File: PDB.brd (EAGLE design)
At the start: 125.9 x 103 mm, 84 parts

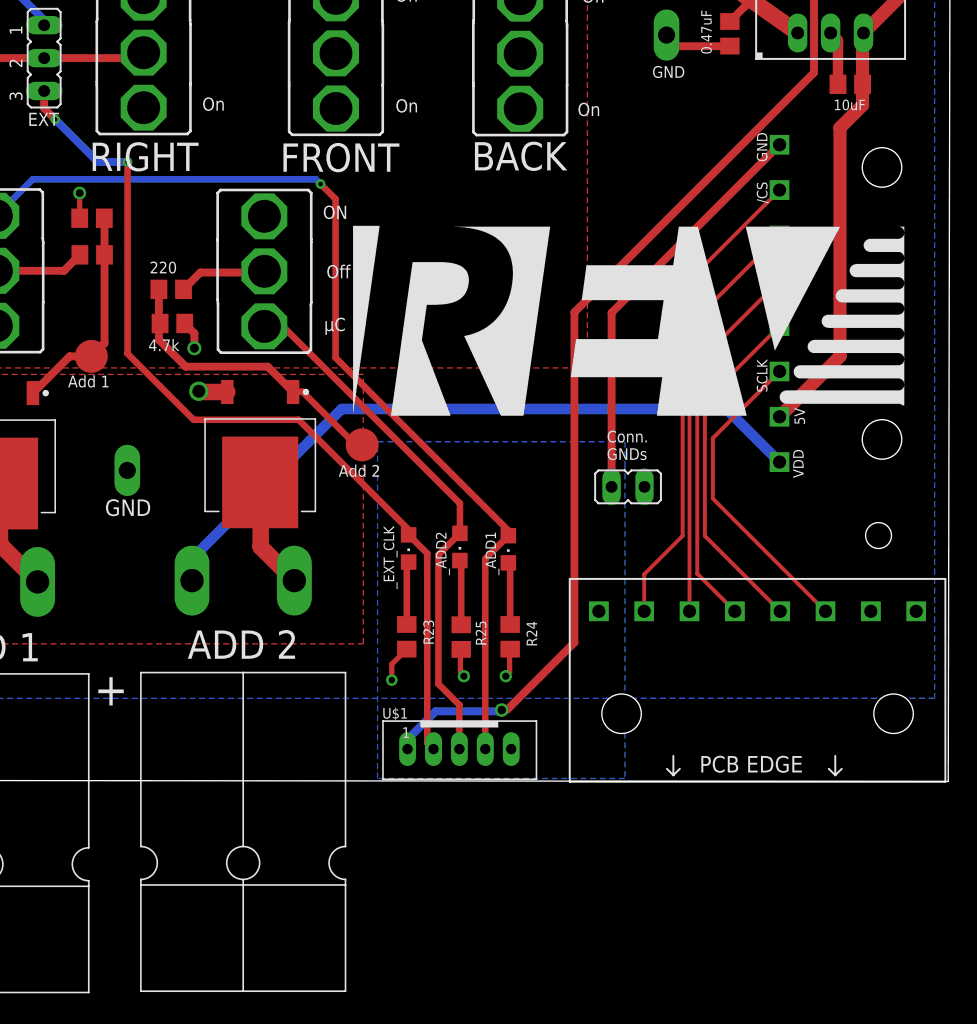
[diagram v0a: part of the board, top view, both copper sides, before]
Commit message: Deleted SPI, ADD2
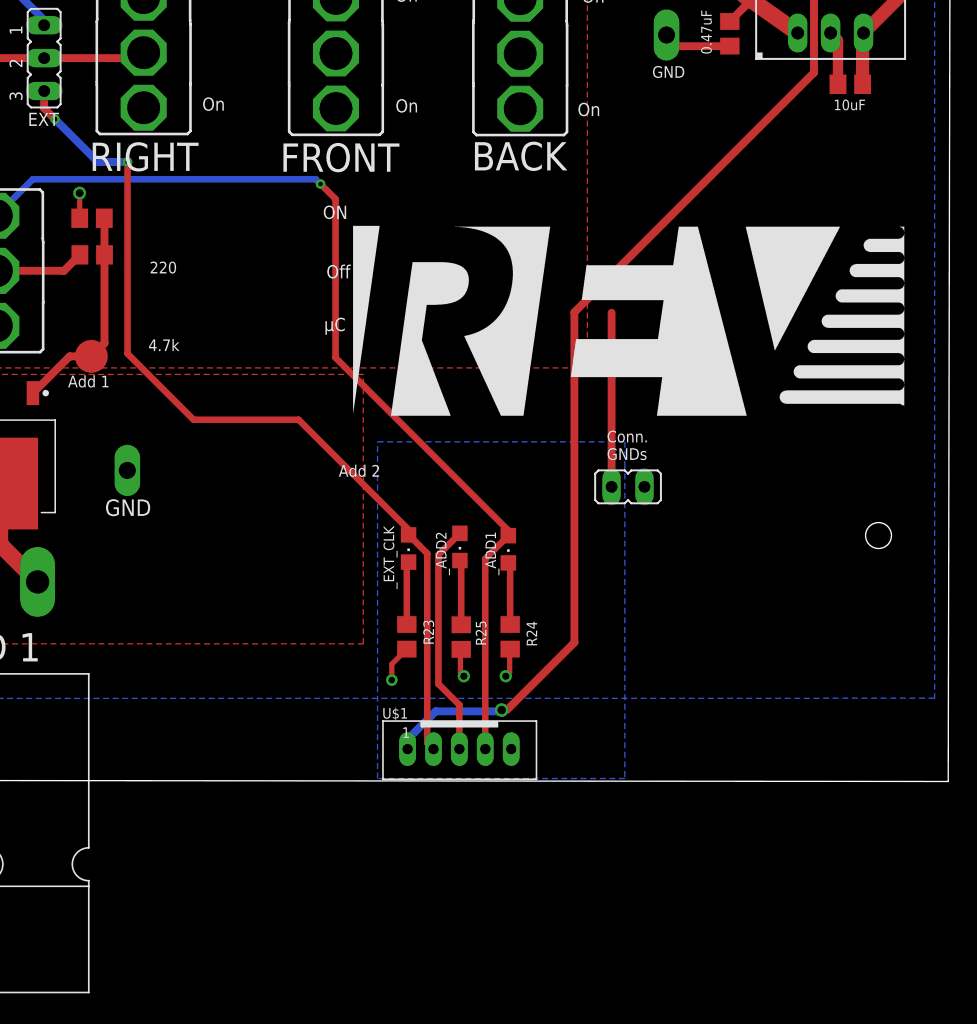
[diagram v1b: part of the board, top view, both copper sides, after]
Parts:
- removed ADD2: NCV8405ADPAK-3PIN, master_library:TO254P1054X240-3
- removed ADD2_: (no value), switch:M9040P
- removed ADD2_OUT: POWERPOLE_POWER25A_HORIZONTAL_G2, powerpoles:POWERPOLE_PAIR_25A_HORIZ_G2
- removed R1: 4.7K, rcl:R0805
- removed R12: 220, rcl:R0805
- removed SPI_IN, SPI_OUT: 8-PIN-MOLEX-RA-FEMALE, master_library:8-PIN-MOLEX
- removed TP2: PTR1B2,54, testpad:B2,54
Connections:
- removed net /CS: SPI_IN.P2, SPI_OUT.P2
- removed net DC: SPI_IN.P4, SPI_OUT.P4
- removed net D_RST: SPI_IN.P3, SPI_OUT.P3
- removed net H6: ADD2_.2, R12.1
- removed net MOSI: SPI_IN.P5, SPI_OUT.P5
- removed net N$7: ADD2.1, R1.1, R12.2, TP2.TP
- removed net N$8: ADD2.3, ADD2_OUT.BLACK
- removed net SCLK: SPI_IN.P6, SPI_OUT.P6
- removed net µC_5V: SPI_IN.P7
- net 10V_REG: no longer ADD2_.3
- net 5V_REG: no longer SPI_OUT.P7
- net GND: no longer ADD2.2, R1.2
- net VDD: no longer ADD2_OUT.RED, SPI_OUT.P8
- net µC_ADD_2: no longer ADD2_.1
- net µC_GND: no longer SPI_IN.P1, SPI_OUT.P1
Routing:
- net VDD: track 76.0 -> 22.5 mm
- net /CS: track 36.8 -> 0.00 mm
- net D_RST: track 31.9 -> 0.00 mm
- net DC: track 29.4 -> 0.00 mm
- net 5V_REG: track 62.0 -> 33.7 mm
- net MOSI: track 26.8 -> 0.00 mm
- net SCLK: track 24.3 -> 0.00 mm
- net µC_ADD_2: track 41.1 -> 18.0 mm
- net N$7: track 23.1 -> 0.00 mm
- net µC_GND: track 39.1 -> 20.8 mm
- net N$8: track 8.67 -> 0.00 mm
- net H6: track 6.82 -> 0.00 mm
- net GND: track 94.1 -> 89.7 mm, vias 22 -> 20
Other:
- board text removed: "/CS"
- board text removed: "5V"
- board text removed: "5V IN"
- board text removed: "ADD 2"
- board text removed: "DC"
- board text removed: "MOSI"
- board text removed: "N/C"
- board text removed: "RST"
- board text removed: "SCLK"
- board text removed: "SPI OUT"
- board text removed: "VDD"

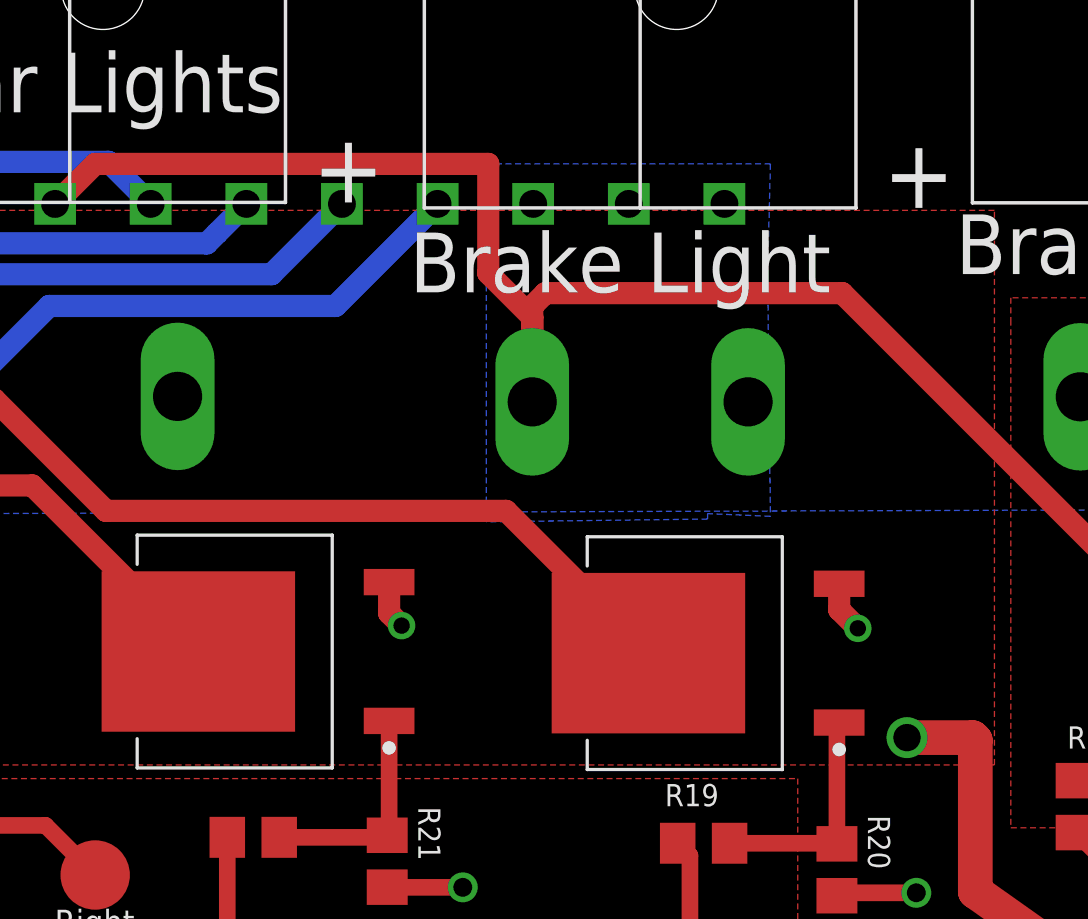
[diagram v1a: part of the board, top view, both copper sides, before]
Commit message: Changed GND to VDD for connector
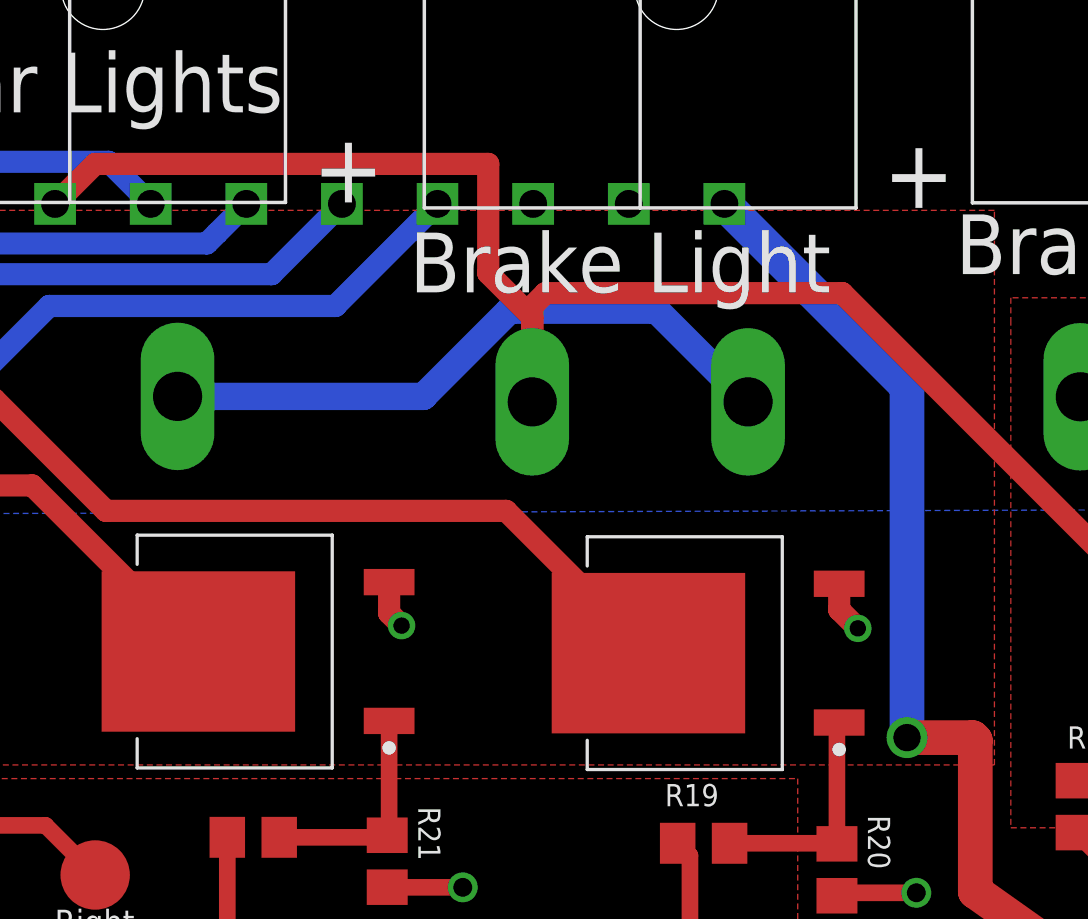
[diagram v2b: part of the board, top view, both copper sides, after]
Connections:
- new net V+: BRAKE_OUT.RED, REARLIGHTS_OUT.RED
- net GND: no longer LIGHTS.P6, LIGHTS.P7, LIGHTS.P8
- net VDD: now also LIGHTS.P6, LIGHTS.P7, LIGHTS.P8; no longer BRAKE_OUT.RED, REARLIGHTS_OUT.RED
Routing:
- net V+: track 0.00 -> 23.6 mm
- net VDD: track 22.5 -> 44.8 mm
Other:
- board text removed: "SPI IN"
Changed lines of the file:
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@@
 <text x="68.1" y="77" size="0.9" layer="25">4.7k</text>
 <text x="48.1" y="77" size="0.9" layer="25">4.7k</text>
-<text x="118.4" y="47" size="1.778" layer="26" rot="MR0">SPI IN</text>
 <text x="104.7" y="55" size="0.8128" layer="26" rot="MR0">µC GND</text>
 <text x="121" y="95.6" size="0.8128" layer="25">10uF</text>
@@
 <contactref element="HAZL_OUT" pad="RED"/>
 <contactref element="HAZR_OUT" pad="RED"/>
-<contactref element="BRAKE_OUT" pad="RED"/>
 <contactref element="HEADLIGHTS_OUT" pad="RED"/>
 <contactref element="C10" pad="+"/>
@@
 <contactref element="WIPER_OUT" pad="RED"/>
 <contactref element="D2" pad="C"/>
-<contactref element="REARLIGHTS_OUT" pad="RED"/>
 <polygon width="0.3048" layer="1" isolate="0.254" rank="2">
 <vertex x="5.7" y="75.2"/>
@@
 <wire x1="114.279484375" y1="103.729484375" x2="114.279484375" y2="104.371015625" width="0.6096" layer="1"/>
 <contactref element="POWER" pad="A"/>
+<contactref element="LIGHTS" pad="P6"/>
+<contactref element="LIGHTS" pad="P7"/>
+<contactref element="LIGHTS" pad="P8"/>
+<wire x1="106" y1="114.1" x2="106" y2="126.952" width="1.27" layer="16"/>
+<wire x1="106" y1="126.952" x2="99.316" y2="133.636" width="1.27" layer="16"/>
 </signal>
 <signal name="N$17">
@@
 <contactref element="TP11" pad="TP"/>
 <contactref element="TP12" pad="TP"/>
-<contactref element="LIGHTS" pad="P8"/>
 <via x="89.74" y="108.62" extent="1-16" drill="0.69"/>
 <via x="106.34" y="108.42" extent="1-16" drill="0.69"/>
@@
 <wire x1="45.4" y1="94" x2="44.6352" y2="94.7648" width="0.8128" layer="1"/>
 <via x="45.4" y="94" extent="1-16" drill="0.6"/>
-<polygon width="0.2032" layer="16" isolate="0.254">
-<vertex x="90.6" y="122"/>
-<vertex x="90.6" y="131"/>
-<vertex x="90.6" y="131.1"/>
-<vertex x="90.6" y="135.1"/>
-<vertex x="101" y="135.1"/>
-<vertex x="100.9" y="131.1"/>
-<vertex x="100.9" y="131"/>
-<vertex x="101" y="122.2"/>
-<vertex x="98.7" y="122.3"/>
-<vertex x="98.7" y="122.1"/>
-</polygon>
-<contactref element="LIGHTS" pad="P7"/>
-<contactref element="LIGHTS" pad="P6"/>
 <wire x1="62.806" y1="87.26" x2="62.806" y2="89.194" width="0.4064" layer="1"/>
 <wire x1="19.244" y1="106.456" x2="20.768" y2="106.456" width="0.6096" layer="1"/>
@@
 <wire x1="113" y1="100.55" x2="112.9896" y2="100.5396" width="1.016" layer="1"/>
 </signal>
+<signal name="V+">
+<contactref element="BRAKE_OUT" pad="RED"/>
+<contactref element="REARLIGHTS_OUT" pad="RED"/>
+<wire x1="79.3" y1="126.59" x2="88.300175" y2="126.59" width="1" layer="16"/>
+<wire x1="88.300175" y1="126.59" x2="91.452575" y2="129.7424" width="1" layer="16"/>
+<wire x1="91.452575" y1="129.7424" x2="96.8296" y2="129.7424" width="1" layer="16"/>
+<wire x1="96.8296" y1="129.7424" x2="100.182" y2="126.39" width="1" layer="16"/>
+</signal>
 </signals>

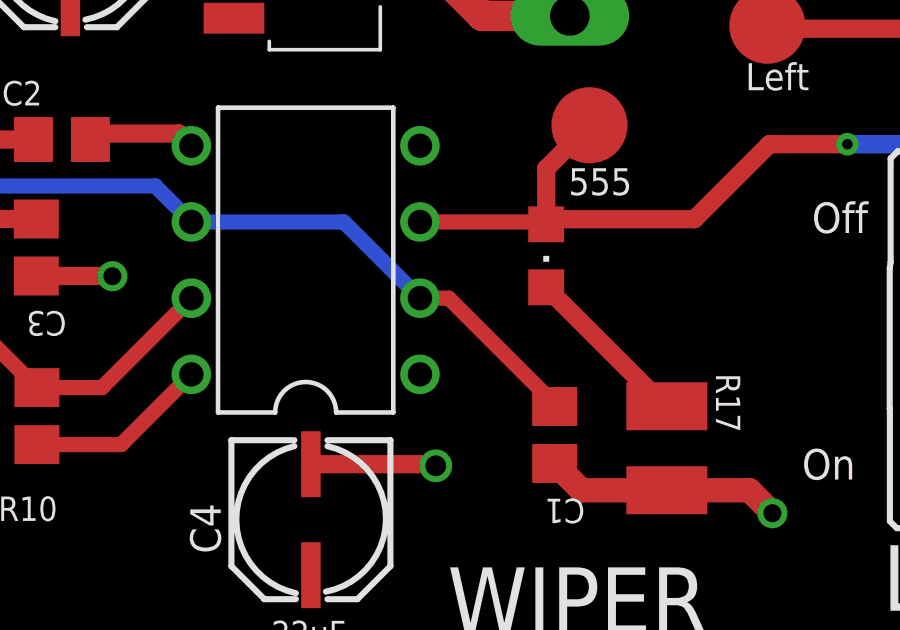
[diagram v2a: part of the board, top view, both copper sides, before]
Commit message: Disconnected 555-timer from the jumper
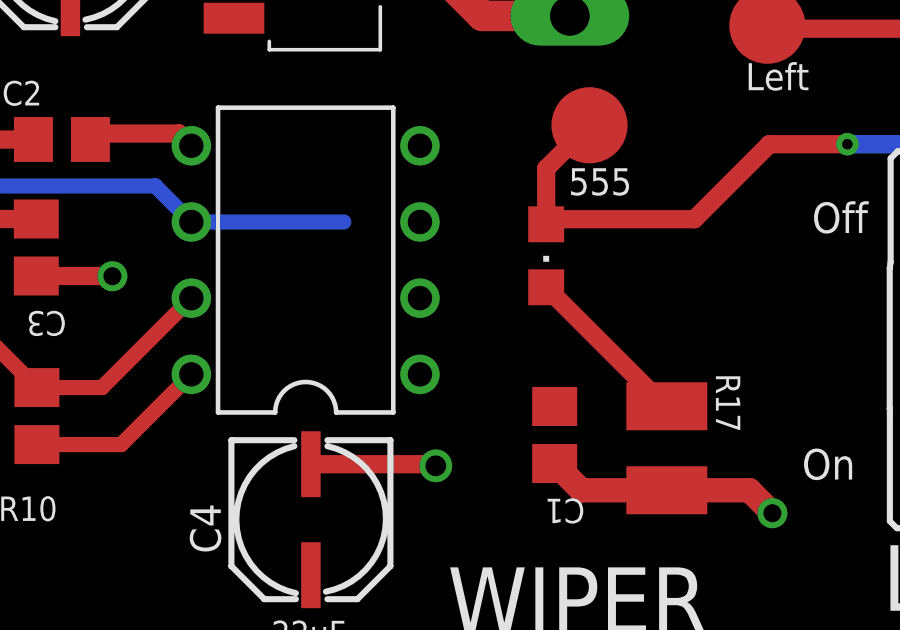
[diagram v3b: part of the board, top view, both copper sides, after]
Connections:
- net 555_OUT: no longer 555.3
- net TR/THR: no longer 555.2, C1.1
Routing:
- net TR/THR: track 39.3 -> 29.6 mm
- net 555_OUT: track 33.5 -> 29.3 mm
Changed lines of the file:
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@@
 <contactref element="JP2" pad="1"/>
 <contactref element="555_CLK_LED" pad="A"/>
-<contactref element="555" pad="3"/>
-<wire x1="33.652" y1="103.708" x2="37.782" y2="103.708" width="0.508" layer="1"/>
 <wire x1="37.86" y1="103.63" x2="37.782" y2="103.708" width="0.6096" layer="1"/>
 <wire x1="38.03" y1="103.8" x2="37.86" y2="103.63" width="0.508" layer="1"/>
@@
 </signal>
 <signal name="TR/THR">
-<contactref element="C1" pad="1"/>
 <contactref element="C3" pad="1"/>
 <contactref element="R11" pad="S"/>
-<contactref element="555" pad="2"/>
 <contactref element="555" pad="6"/>
-<wire x1="38.143621875" y1="97.635378125" x2="38.1436" y2="97.5566" width="0.6096" layer="1"/>
 <wire x1="18.388" y1="104.907" x2="24.833" y2="104.907" width="0.508" layer="16"/>
 <wire x1="24.833" y1="104.907" x2="26.032" y2="103.708" width="0.508" layer="16"/>
 <wire x1="26.032" y1="103.708" x2="31.112" y2="103.708" width="0.508" layer="16"/>
-<wire x1="31.112" y1="103.708" x2="33.652" y2="101.168" width="0.508" layer="16"/>
-<wire x1="33.652" y1="101.168" x2="34.611" y2="101.168" width="0.508" layer="1"/>
-<wire x1="34.611" y1="101.168" x2="38.143621875" y2="97.635378125" width="0.508" layer="1"/>
 <wire x1="20.863" y1="103.807" x2="17.688" y2="103.807" width="0.6096" layer="1"/>
 <wire x1="17.688" y1="103.807" x2="13.588" y2="107.907" width="0.6096" layer="1"/>
